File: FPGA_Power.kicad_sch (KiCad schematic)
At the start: 29 parts, among them U11 LIFCL-40-9BG256C

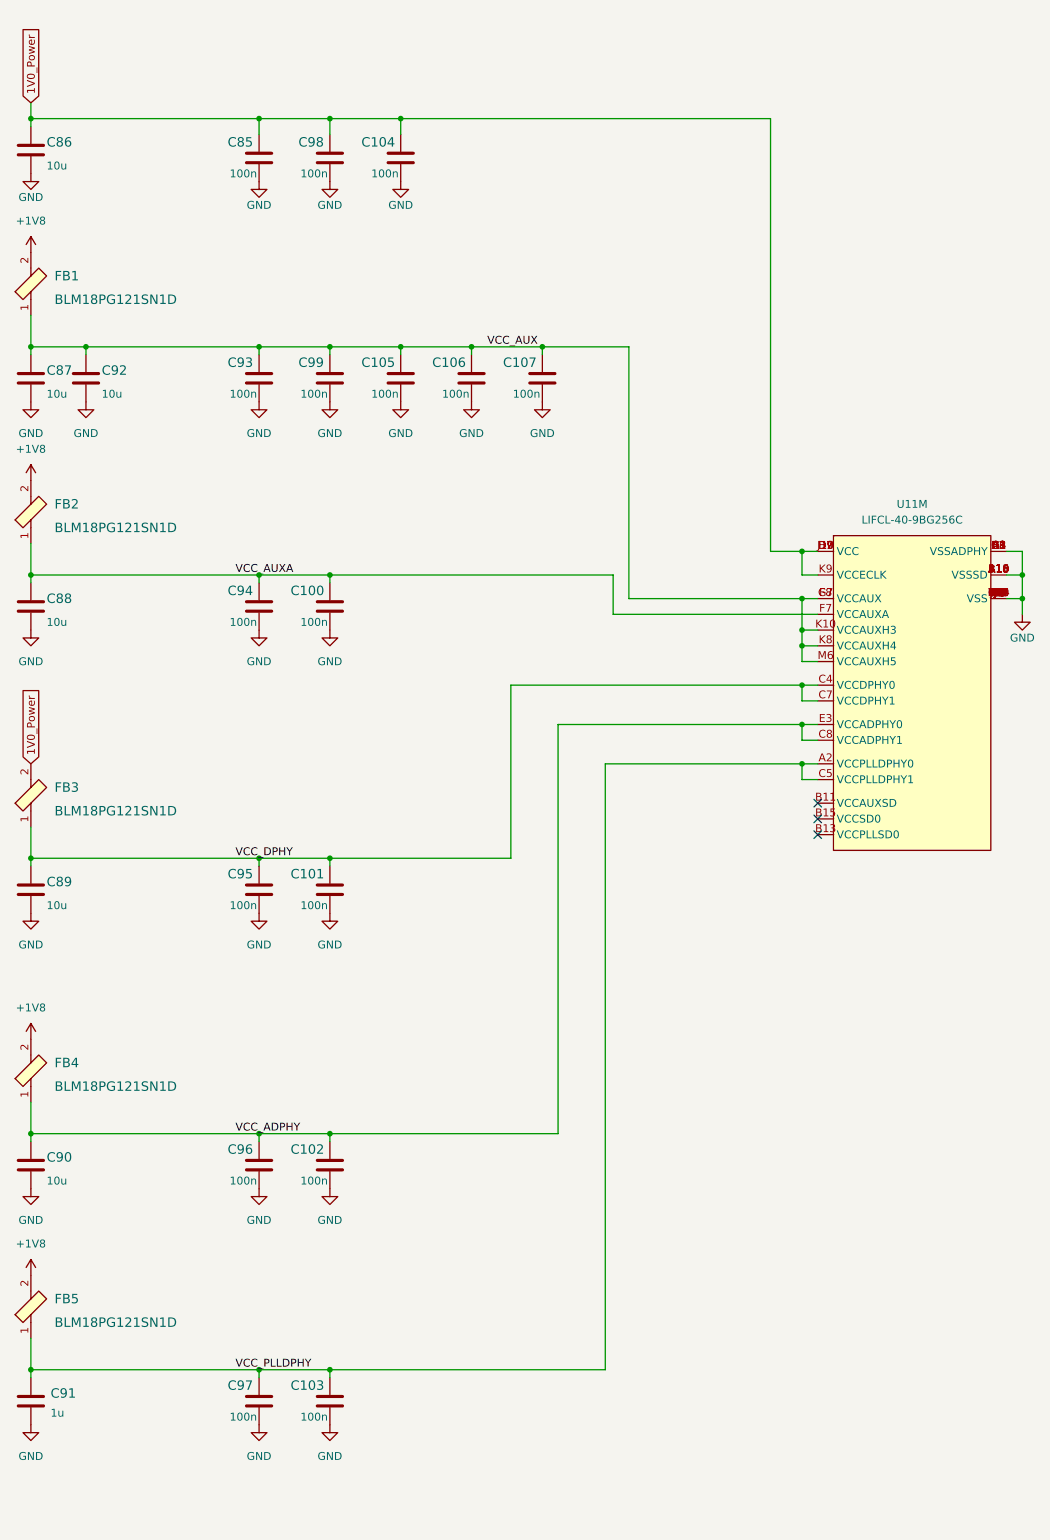
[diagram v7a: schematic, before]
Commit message: Fix FPGA power supply
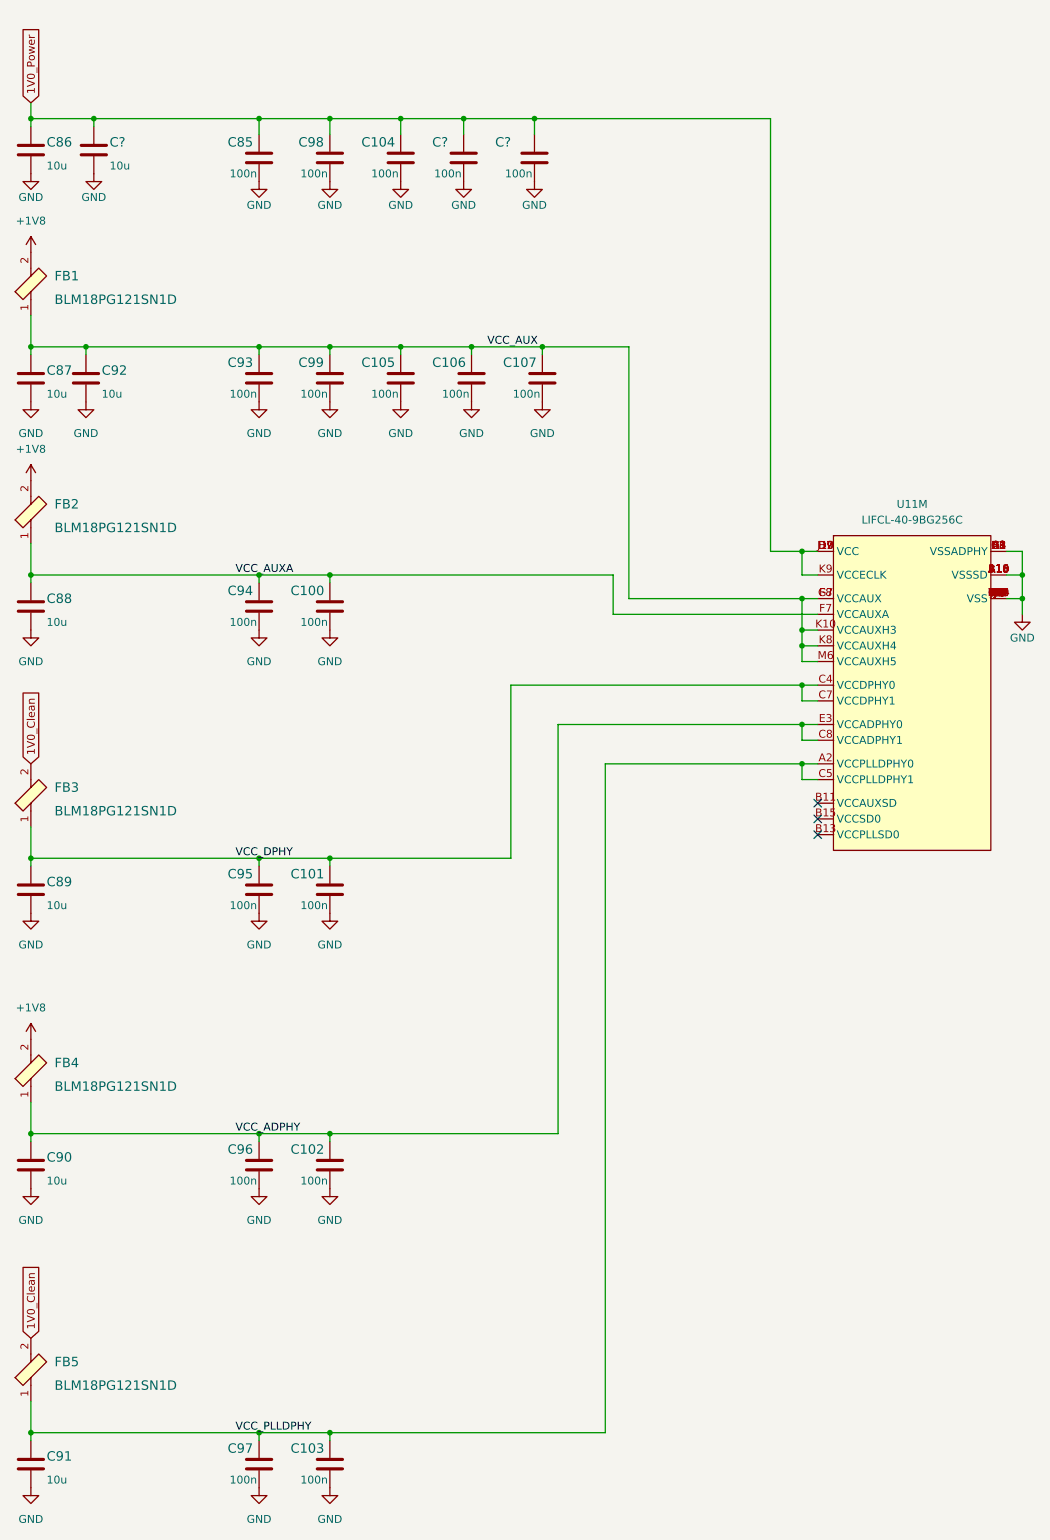
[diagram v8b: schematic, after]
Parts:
- removed C91: C_1u_0603, crosslink-nx-video-converter-footprints:0603-cap, symbol crosslink-nx-video-converter:C_1u_0603
- added C91, C?: C_10u_0603, crosslink-nx-video-converter-footprints:0603-cap, symbol crosslink-nx-video-converter:C_10u_0603
- added C? (x2): C_100n_0402, crosslink-nx-video-converter-footprints:0402-cap, symbol crosslink-nx-video-converter:C_100n_0402
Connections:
- net +1V8: no longer FB5.2
- net 1V0_Power: now also C?.1, C?.1, C?.1; no longer FB3.2
- net GND: now also C91.2, C?.2, C?.2, C?.2
- net VCC_PLLDPHY: now also C91.1
- new net 1V0_Clean: FB3.2, FB5.2
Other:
- moved on the sheet: C103, C97, FB5
